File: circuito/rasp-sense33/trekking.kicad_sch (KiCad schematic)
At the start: 22 parts, among them J1 Raspberry Pi, J10 MOTOR, J12 I2C0, J13 I2C0, J14 I2C0, J15 I2C0, J16 I2C0, J17 I2C0, J18 Module, J2 ENCODER, J3 ENCODER, J4 ENCODER, J5 ENCODER, J6 POWER, J9 MOTOR, U1 RPI-PICO, U2 AMS1117-3.3

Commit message: driver motor rev 2
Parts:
- removed J6: POWER, symbol Connector:Conn_01x06_Female
- added J11, J19, J20: OUT, MyFootprint:CONN5mm-3, symbol Connector:Conn_01x03_Female
- added J21, J22: INPUT, MyFootprint:CONN5mm-3, symbol Connector:Conn_01x03_Female
- added J6: VIN, MyFootprint:AK300-2, symbol Connector:Conn_01x02_Female
- added J7: VCC, MyFootprint:AK300-2, symbol Connector:Conn_01x02_Female
- added J8: 5VIN, MyFootprint:AK300-2, symbol Connector:Conn_01x02_Female
- added R1, R10, R11, R12, R13, R4, R6, R8, R9: 10K, Resistor_SMD:R_0805_2012Metric_Pad1.20x1.40mm_HandSolder, symbol Device:R
- added R14, R15, R16, R17, R18, R19, R2, R5, R7: 1K, Resistor_SMD:R_0805_2012Metric_Pad1.20x1.40mm_HandSolder, symbol Device:R
- added R3: ~0., Resistor_SMD:R_1206_3216Metric_Pad1.30x1.75mm_HandSolder, symbol Device:R
- C1, C2, C3: footprint (none) -> Capacitor_SMD:C_0805_2012Metric_Pad1.18x1.45mm_HandSolder
- U1: footprint trekking-library:RPI_PICO -> MyFootprint:RPI-PICO-SMD
- U3: renamed from U?; footprint (none) -> Package_SO:SOIC-18W_7.5x11.6mm_P1.27mm
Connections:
- net +5V: now also U3.10 (COM), J8.1 (Pin_1), R6.1
- net ADC0: now also R6.2, R7.1
- net ADC1: now also R4.2, R5.1
- net ADC2: now also R1.2, R2.1
- net Earth: now also U1.42 (GND), U3.9 (GND), J20.3 (Pin_3), J6.2 (Pin_2), J7.2 (Pin_2), J8.2 (Pin_2), R14.2, R15.2, R16.2, R17.2, R18.2, R19.2, R2.2, R5.2, R7.2; no longer U1.41 (GND)
- net SWCLK: now also U1.41 (SWCLK); no longer U1.40 (VBUS)
- net SWDIO: now also U1.43 (SWDIO); no longer U1.40 (VBUS)
- net TX: now reaches A1.1 (TX)
- net D7: now reaches A1.10 (D7~)
- net D7: now also U3.6 (I6)
- net D8: now reaches A1.11 (D8~)
- net D8: now also U3.7 (I7)
- net D9: now reaches A1.12 (D9~)
- net D9: now also U3.8 (I8)
- net SC: now reaches A1.13 (D10~)
- net SC: now also J1.24 (Pin_24)
- net MOSI: now reaches A1.14 (D11~/MOSI)
- net MOSI: now also J1.19 (Pin_19)
- net MISO: now reaches A1.15 (D12~/MISO)
- net MISO: now also J1.21 (Pin_21)
- net SCK: now reaches A1.16 (D13~/SCK)
- net SCK: now also J1.23 (Pin_23)
- net A0: now reaches A1.19 (A0)
- net A0: now also R10.2, R16.1
- net RX: now reaches A1.2 (RX)
- net A1: now reaches A1.20 (A1)
- net A1: now also R15.1, R9.2
- net A2: now reaches A1.21 (A2)
- net A2: now also R14.1, R8.2
- net A3: now reaches A1.22 (A3)
- net A3: now also R13.2, R19.1
- net A6: now reaches A1.25 (A6)
- net A6: now also R12.2, R18.1
- net A7: now reaches A1.26 (A7)
- net A7: now also R11.2, R17.1
- net D2: now reaches A1.5 (D2~)
- net D2: now also U3.1 (I1)
- net D3: now reaches A1.6 (D3~)
- net D3: now also U3.2 (I2)
- net D4: now reaches A1.7 (D4~)
- net D4: now also U3.3 (I3)
- net D5: now reaches A1.8 (D5~)
- net D5: now also U3.4 (I4)
- net D6: now reaches A1.9 (D6~)
- net D6: now also U3.5 (I5)
- net O9: now reaches U3.11 (O8)
- net O9: now also J11.1 (Pin_1)
- net O8: now reaches U3.12 (O7)
- net O8: now also J11.2 (Pin_2)
- net O7: now reaches U3.13 (O6)
- net O7: now also J11.3 (Pin_3)
- net O6: now reaches U3.14 (O5)
- net O6: now also J19.1 (Pin_1)
- net O5: now reaches U3.15 (O4)
- net O5: now also J19.2 (Pin_2)
- net O4: now reaches U3.16 (O3)
- net O4: now also J19.3 (Pin_3)
- net O3: now reaches U3.17 (O2)
- net O3: now also J20.1 (Pin_1)
- net O2: now reaches U3.18 (O1)
- net O2: now also J20.2 (Pin_2)
- new net: J22.3 (Pin_3), R13.1
- new net: J21.2 (Pin_2), R9.1
- new net: J22.1 (Pin_1), R11.1
- new net: J21.1 (Pin_1), R8.1
- new net: J21.3 (Pin_3), R10.1
- new net: J22.2 (Pin_2), R12.1
- new net VCC: J7.1 (Pin_1), R3.2, R4.1
- new net VIN: J6.1 (Pin_1), R1.1, R3.1
- no-connect marks 27 -> 23
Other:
- note added: "DRIVER"
- moved on the sheet: C1, C2, C3, J1, U1, U2, U3

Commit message: driver motor rev 2
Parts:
- removed C1: 100nF, Capacitor_SMD:C_0805_2012Metric_Pad1.18x1.45mm_HandSolder, symbol Device:C
- removed U2: AMS1117-3.3, Package_TO_SOT_SMD:SOT-223-3_TabPin2, symbol Regulator_Linear:AMS1117-3.3
- added J23: ENCODER, Connector_Molex:Molex_KK-254_AE-6410-04A_1x04_P2.54mm_Vertical, symbol Connector:Conn_01x04_Male
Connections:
- net +3V3: now also J23.1 (Pin_1); no longer C2.1, C3.1
- net +5V: now also C2.1, C3.1
- net Earth: now also J23.2 (Pin_2)
- net G22: now also J1.33 (Pin_33); no longer J1.29 (Pin_29)
- net P3C: now also J4.2 (Pin_2); no longer J5.2 (Pin_2)
- net P3D: now also J5.2 (Pin_2); no longer J4.2 (Pin_2)
- net RST_A: now also J1.26 (Pin_26); no longer A1.28 (~{RESET}), J1.33 (Pin_33)
- net RXD1: now also J18.7 (Pin_7); no longer J18.8 (Pin_8)
- net TXD1: now also J18.8 (Pin_8); no longer J18.7 (Pin_7)
- net RX renamed ARX
- net ARX: now also J23.4 (Pin_4)
- net TX renamed ATX
- net ATX: now also J23.3 (Pin_3)
- no-connect marks 23 -> 24

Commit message: driver rasp-sense33
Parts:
- removed J18: Module, Connector_PinHeader_2.54mm:PinHeader_1x08_P2.54mm_Vertical, symbol Connector:Conn_01x08_Male
- added C1, C6: 100nF, Capacitor_SMD:C_0805_2012Metric_Pad1.18x1.45mm_HandSolder, symbol Device:C
- added C4: 100uF50V, Capacitor_SMD:CP_Elec_8x10, symbol Device:C_Polarized
- added C5: 220uF35V, Capacitor_SMD:CP_Elec_8x10, symbol Device:C_Polarized
- added D1: 1N5822, MyFootprint:My_D_MELF-RM10_Universal_Handsoldering_2, symbol Device:D_Zener
- added J18: Module, Connector_PinHeader_2.54mm:PinHeader_1x12_P2.54mm_Vertical, symbol Connector:Conn_01x12_Male
- added L1: 33uH, Inductor_SMD:L_12x12mm_H8mm, symbol Device:L
- added U2: LM2596T-5, Package_TO_SOT_SMD:TO-263-5_TabPin3, symbol Regulator_Switching:LM2596T-5
- J23: value ENCODER -> UART
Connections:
- net +3V3: now also J18.7 (Pin_7)
- net +5V: now also C5.1, C6.1, J18.12 (Pin_12), L1.2, U2.4 (FB); no longer U3.10 (COM)
- net Earth: now also C1.2, C4.2, C5.2, C6.2, D1.2 (A), J18.11 (Pin_11), J18.8 (Pin_8), U2.3 (GND), U2.5 (~{ON}/OFF)
- net G22: now also J1.35 (Pin_35); no longer J1.33 (Pin_33)
- net RUN: now also J1.37 (Pin_37); no longer J1.31 (Pin_31)
- net RXD1: now also J18.2 (Pin_2)
- net SCL0: now also J18.9 (Pin_9)
- net SDA0: now also J18.10 (Pin_10)
- net SPI0_RX: now also J18.3 (Pin_3)
- net SPI0_SC: now also J18.4 (Pin_4)
- net SPI0_SCK: now also J18.5 (Pin_5)
- net SPI0_TX: now also J18.6 (Pin_6)
- net TXD1: now also J18.1 (Pin_1)
- net VCC: now also U3.10 (COM), C1.1, C4.1, U2.1 (VIN)
- new net: D1.1 (K), L1.1, U2.2 (OUT)
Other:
- title: Controle e Alimentação -> Controle e Alimentação e Instrumentação
- moved on the sheet: C2, C3, J10, J12, J13, J14, J15, J16, J17, J2, J23, J3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

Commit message: incluindo movimento
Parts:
- added R20, R21: 0, Resistor_SMD:R_0805_2012Metric_Pad1.20x1.40mm_HandSolder, symbol Device:R
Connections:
- net +5V: now also R21.1; no longer C5.1, C6.1, L1.2, U2.4 (FB)
- net VCC: now also R20.1; no longer C1.1, C4.1, U2.1 (VIN)
- new net: C5.1, C6.1, L1.2, R21.2, U2.4 (FB)
- new net: C1.1, C4.1, R20.2, U2.1 (VIN)
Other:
- moved on the sheet: C2, C3, J11, J19, J20

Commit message: update
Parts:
- J8: value 5VIN -> 5V
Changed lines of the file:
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@@
     (stroke (width 0) (type default) (color 0 0 0 0))
   )
-  (wire (pts (xy 205.74 152.4) (xy 213.36 152.4))
+  (wire (pts (xy 205.74 152.4) (xy 216.535 152.4))
     (stroke (width 0) (type default) (color 0 0 0 0))
   )
@@
     (stroke (width 0) (type default) (color 0 0 0 0))
   )
-  (wire (pts (xy 210.82 157.48) (xy 213.36 157.48))
+  (wire (pts (xy 210.82 157.48) (xy 216.535 157.48))
     (stroke (width 0) (type default) (color 0 0 0 0))
   )
@@
     (stroke (width 0) (type default) (color 0 0 0 0))
   )
-  (wire (pts (xy 208.28 154.94) (xy 213.36 154.94))
+  (wire (pts (xy 208.28 154.94) (xy 216.535 154.94))
     (stroke (width 0) (type default) (color 0 0 0 0))
   )
@@
     (effects (font (size 1.27 1.27)) (justify left bottom))
   )
-  (label "A7" (at 213.36 152.4 0)
+  (label "A7" (at 216.535 152.4 0)
     (effects (font (size 1.27 1.27)) (justify left bottom))
   )
@@
     (effects (font (size 1.27 1.27)) (justify right bottom))
   )
-  (label "A3" (at 213.36 157.48 0)
+  (label "A3" (at 216.535 157.48 0)
     (effects (font (size 1.27 1.27)) (justify left bottom))
   )
@@
     (effects (font (size 1.27 1.27)) (justify right bottom))
   )
-  (label "A6" (at 213.36 154.94 0)
+  (label "A6" (at 216.535 154.94 0)
     (effects (font (size 1.27 1.27)) (justify left bottom))
   )
@@
       (effects (font (size 1.27 1.27)) (justify right))
     )
-    (property "Value" "5VIN" (id 1) (at 36.83 26.67 90)
+    (property "Value" "5V" (id 1) (at 38.1 26.67 90)
       (effects (font (size 1.27 1.27)) (justify right))
     )
@@
   (symbol (lib_id "Regulator_Switching:LM2596T-5") (at 60.96 73.66 0) (unit 1)
     (in_bom yes) (on_board yes)
-    (property "Reference" "U2" (id 0) (at 60.96 64.77 0))
+    (property "Reference" "U2" (id 0) (at 60.96 65.405 0))
     (property "Value" "LM2596T-5" (id 1) (at 60.96 67.31 0))
     (property "Footprint" "Package_TO_SOT_SMD:TO-263-5_TabPin3" (id 2) (at 62.23 80.01 0)
@@
     )
     (path "/029dbe07-57dc-407b-81a5-7a1f006f9bcd"
-      (reference "J8") (unit 1) (value "5VIN") (footprint "MyFootprint:AK300-2")
+      (reference "J8") (unit 1) (value "5V") (footprint "MyFootprint:AK300-2")
     )
     (path "/f1567048-d8e3-4cca-8c2e-84408962c0df"

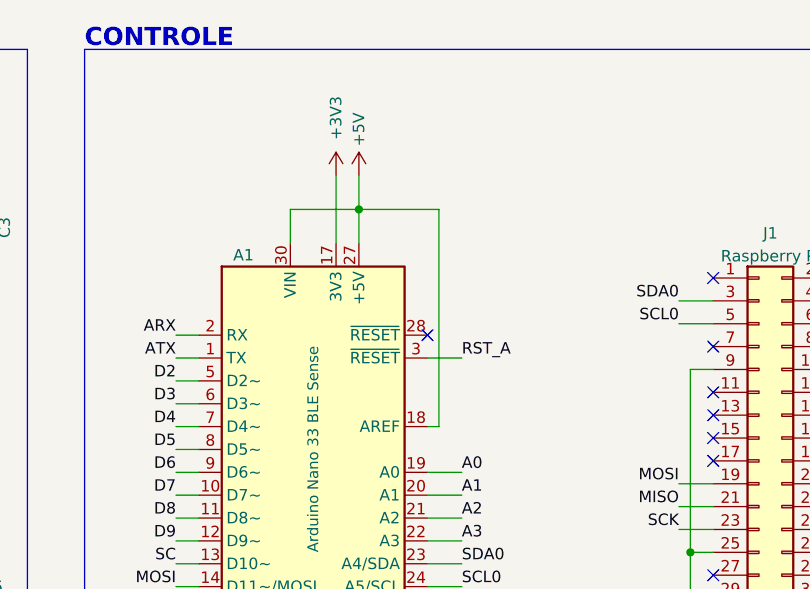
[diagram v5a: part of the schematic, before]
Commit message: correção AREF PCI
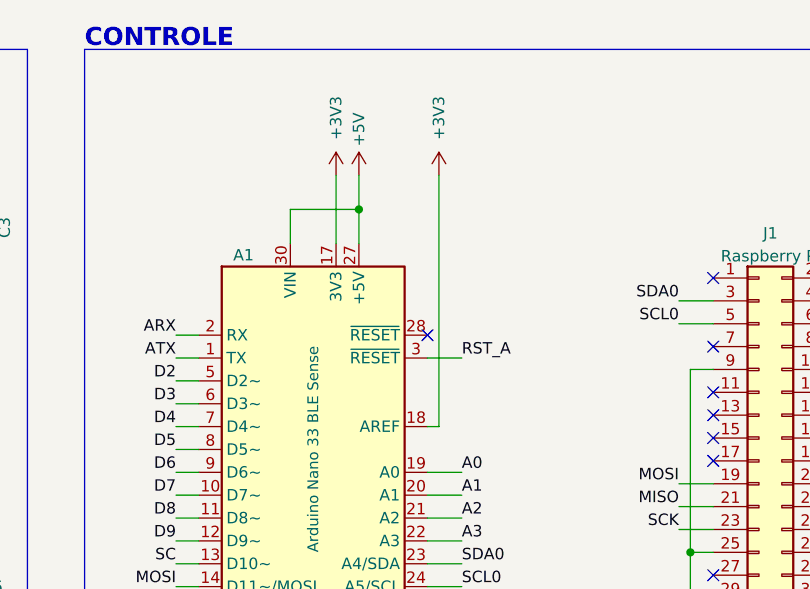
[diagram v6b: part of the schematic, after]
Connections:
- net +3V3: now also A1.18 (AREF)
- net +5V: no longer A1.18 (AREF)
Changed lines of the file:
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@@
     (stroke (width 0) (type default) (color 0 0 0 0))
   )
-  (wire (pts (xy 154.94 62.23) (xy 154.94 38.1))
-    (stroke (width 0) (type default) (color 0 0 0 0))
-  )
   (wire (pts (xy 52.07 110.49) (xy 52.07 118.11))
     (stroke (width 0) (type default) (color 0 0 0 0))
@@
     (stroke (width 0) (type default) (color 0 0 0 0))
   )
-  (wire (pts (xy 154.94 38.1) (xy 146.05 38.1))
-    (stroke (width 0) (type default) (color 0 0 0 0))
-  )
   (wire (pts (xy 71.12 110.49) (xy 71.12 113.03))
     (stroke (width 0) (type default) (color 0 0 0 0))
@@
     (stroke (width 0) (type default) (color 0 0 0 0))
   )
-  (wire (pts (xy 143.51 34.29) (xy 143.51 41.91))
-    (stroke (width 0) (type default) (color 0 0 0 0))
-  )
   (wire (pts (xy 38.1 110.49) (xy 38.1 118.11))
     (stroke (width 0) (type default) (color 0 0 0 0))
@@
     (stroke (width 0) (type default) (color 0 0 0 0))
   )
+  (wire (pts (xy 143.51 34.29) (xy 143.51 41.91))
+    (stroke (width 0) (type default) (color 0 0 0 0))
+  )
   (wire (pts (xy 39.37 171.45) (xy 39.37 173.99))
     (stroke (width 0) (type default) (color 0 0 0 0))
@@
     (stroke (width 0) (type default) (color 0 0 0 0))
   )
+  (wire (pts (xy 154.94 34.29) (xy 154.94 62.23))
+    (stroke (width 0) (type default) (color 0 0 0 0))
+  )
   (wire (pts (xy 200.66 45.72) (xy 200.66 48.26))
     (stroke (width 0) (type default) (color 0 0 0 0))
@@
     (pin "1")
   )
+  (symbol (lib_id "power:+3V3") (at 154.94 34.29 0) (unit 1)
+    (in_bom yes) (on_board yes)
+    (property "Reference" "#PWR?" (id 0) (at 154.94 38.1 0)
+      (effects (font (size 1.27 1.27)) hide)
+    )
+    (property "Value" "+3V3" (id 1) (at 154.94 27.94 90))
+    (property "Footprint" "" (id 2) (at 154.94 34.29 0)
+      (effects (font (size 1.27 1.27)) hide)
+    )
+    (property "Datasheet" "" (id 3) (at 154.94 34.29 0)
+      (effects (font (size 1.27 1.27)) hide)
+    )
+    (pin "1")
+  )
   (symbol (lib_id "Device:R") (at 210.82 163.83 0) (unit 1)
     (in_bom yes) (on_board yes)
@@
       (reference "#PWR0156") (unit 1) (value "+5V") (footprint "")
     )
+    (path "/b6699bba-8f98-45da-ac31-fc88e957e309"
+      (reference "#PWR?") (unit 1) (value "+3V3") (footprint "")
+    )
     (path "/0cdfb3f1-316e-4447-a791-14eba7b92039"
